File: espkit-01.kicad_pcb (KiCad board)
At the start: 2 copper layers, 20 x 25 mm, 14 parts, among them IC1 WS2812B, P1 ESP-01, P2 BREAKOUT, P3 SERIAL, P4 PWR, P5 NEOPIXEL, P6 BRIDGE, SW1 RESET, SW2 PRGM

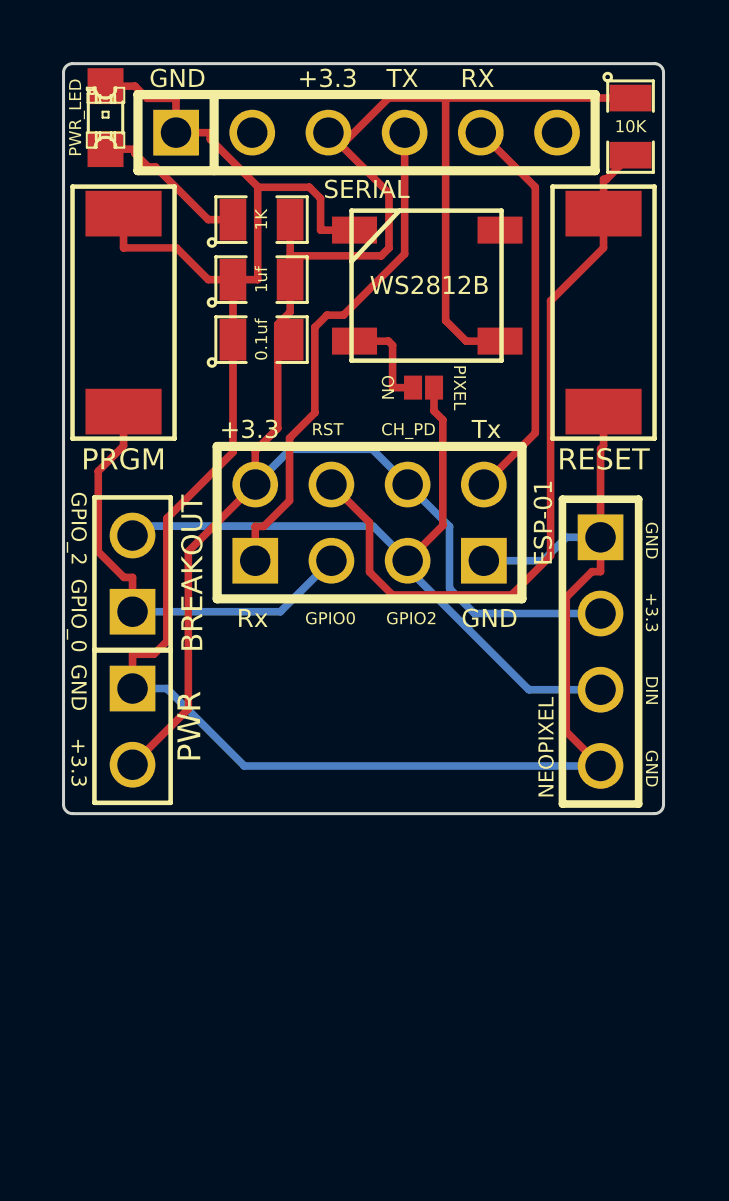
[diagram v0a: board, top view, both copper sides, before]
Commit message: Redundant power led removed
bridge connection now easy to get too.
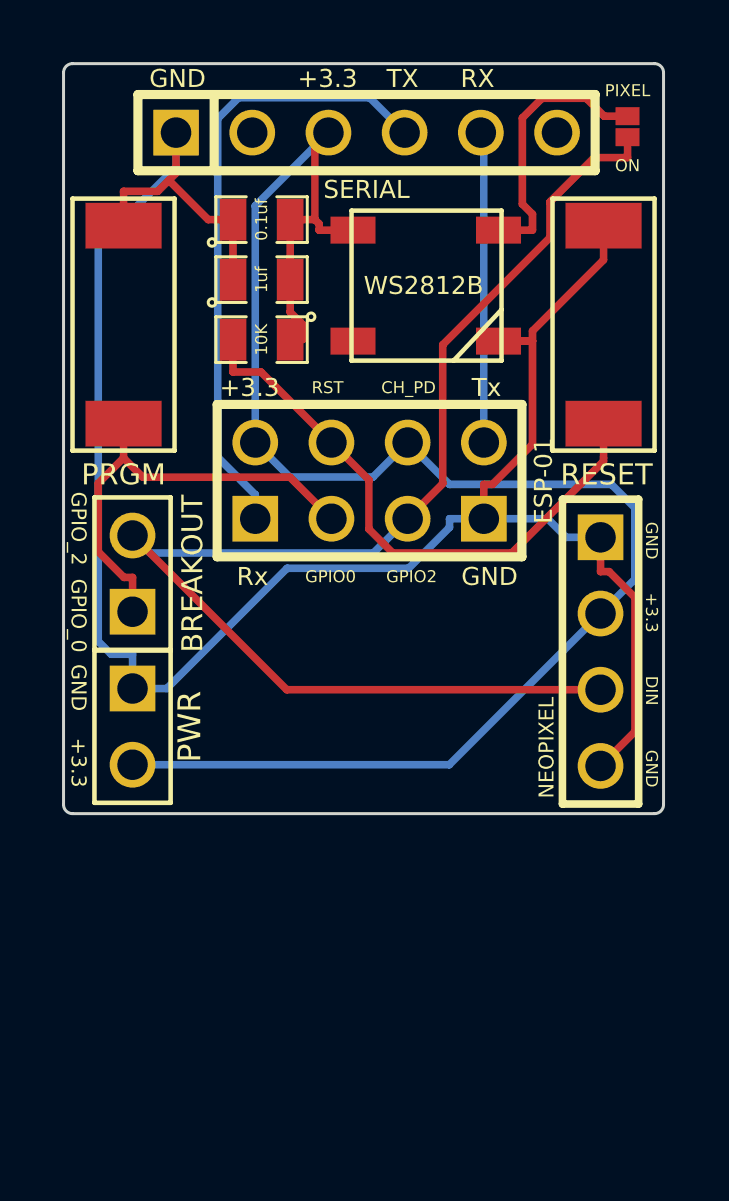
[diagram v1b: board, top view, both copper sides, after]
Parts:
- removed D1: PWR_LED, LED-0805
- removed R3: 1K, SM0805
- moved R1 14.2 mm to (18.7, 21.3), turned to 180 degrees
- moved P6 11.0 mm to (30.9, 14.2), turned to 90 degrees
- moved C2 4.00 mm to (18.7, 17.3)
- moved P1 1.40 mm to (22.3, 26.0)
- moved SW1 0.40 mm to (30.1, 20.8), turned to 270 degrees
- moved SW2 0.40 mm to (14.1, 20.8)
- turned IC1 to 0 degrees
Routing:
- net GPIO2: track 24.5 -> 44.0 mm
- net +3.3V: track 64.1 -> 57.6 mm
- net N-000004: track 3.42 -> 9.03 mm
- net N-0000012: track 24.9 -> 19.4 mm
- net N-000006: track 5.31 -> 0.00 mm
- net TX: track 16.8 -> 21.6 mm
- net RX: track 13.2 -> 10.4 mm
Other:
- board text added: "ESPkit-01 V1.2 https://github.com/mage0r/ESPkit-01 John Spencer & Andy Gelme, 2015 Made at hackmelbourne.org"
- board text removed: "ESPkit-01 V1.1 https://github.com/mage0r/ESPkit-01 John Spencer & Andy Gelme, 2015 Made at hackmelbourne.org"

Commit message: New Design with auto program.
You should be able to do away with the serial/usb programmer and just use the NodeMCU v1.0 board in Arduino to auto-program.
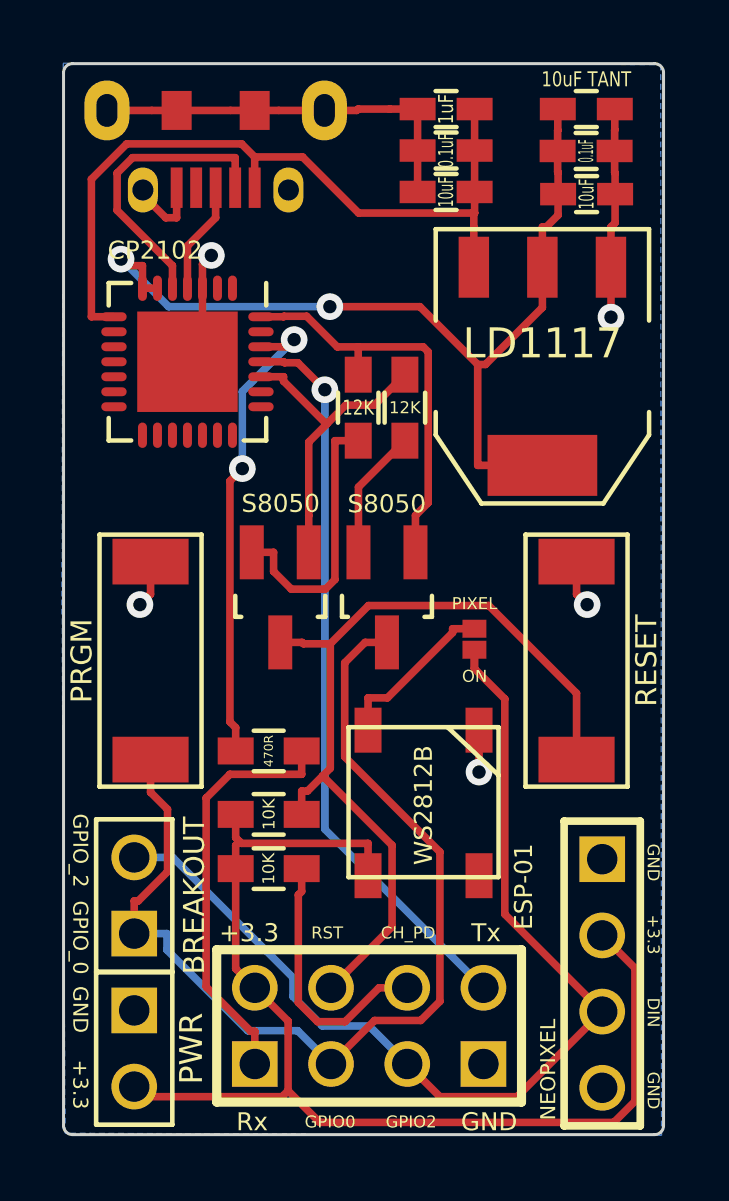
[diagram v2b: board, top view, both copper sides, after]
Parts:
- removed C2: 0.1uf, SM0805
- removed C3: 1uf, SM0805
- added C1: 10uF, Capacitors_SMD:C_0603_HandSoldering, F.Cu at (29.5, 16.4)
- added C4: 0.1uF, Capacitors_SMD:C_0603_HandSoldering, F.Cu at (29.5, 15.0)
- added C5: 1uF, Capacitors_SMD:C_0603_HandSoldering, F.Cu at (24.9, 13.6)
- added C6: 10uF, Capacitors_SMD:C_0603_HandSoldering, F.Cu at (24.9, 16.4)
- added C7: 0.1uF, Capacitors_SMD:C_0603_HandSoldering, F.Cu at (24.9, 15.0)
- added C8: 10uF TANT, Capacitors_SMD:C_0603_HandSoldering, F.Cu at (29.5, 13.6)
- added Q1: S8050, TO_SOT_Packages_SMD:SOT-23_Handsoldering, F.Cu at (19.3, 29.9)
- added Q2: S8050, TO_SOT_Packages_SMD:SOT-23_Handsoldering, F.Cu at (22.9, 29.9)
- added R2: 12K, Resistors_SMD:R_0603_HandSoldering, F.Cu at (21.9, 23.6)
- added R3: 12K, Resistors_SMD:R_0603_HandSoldering, F.Cu at (23.5, 23.6)
- added R4: 10K, Resistors_SMD:R_0603_HandSoldering, F.Cu at (18.9, 37.1)
- added R5: 470R, Resistors_SMD:R_0603_HandSoldering, F.Cu at (18.9, 35.0)
- added U1: LD1117, TO_SOT_Packages_SMD:SOT-223, F.Cu at (28.1, 22.2)
- added U2: CP2102, Housings_DFN_QFN:QFN-28-1EP_5x5mm_Pitch0.5mm, F.Cu at (16.2, 22.0)
- P3: value SERIAL -> USB_5PIN_SHELL; footprint PIN_ARRAY-6X1 -> freetronics_footprints:USB-MICRO-5pin_PTHMOUNT
- R1: footprint SM0805 -> Resistors_SMD:R_0603_HandSoldering
- moved P1 18.2 mm to (22.3, 44.2)
- moved P6 17.8 mm to (25.8, 31.3)
- moved R1 17.6 mm to (18.9, 38.9)
- moved IC1 17.2 mm to (24.1, 36.7), turned to 90 degrees
- moved SW1 11.2 mm to (29.2, 32.0)
- moved SW2 11.2 mm to (15.0, 32.0), turned to 270 degrees
- moved P5 10.7 mm to (30.1, 42.4)
- moved P2 10.7 mm to (14.5, 39.8)
- moved P4 10.7 mm to (14.5, 44.9)
- moved P3 5.35 mm to (17.2, 16.2), turned to 270 degrees
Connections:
- net GPIO2 renamed /GPIO2
- IC1 pad 2: (no net) -> Net-(IC1-Pad2)
- P1 pad 1: TX -> /TXD
- P1 pad 3: GPIO0 -> /GPIO0
- P1 pad 4: N-0000012 -> /RESET
- P1 pad 6: +3.3V -> /ESP_EN
- P1 pad 8: RX -> /RXD
- P2 pad 1: GPIO0 -> /GPIO0
- P3 pad 1: GND -> +5V
- P3 pad 2: (no net) -> /USB_D-
- P3 pad 3: +3.3V -> /USB_D+
- P3 pad 4: TX -> Net-(P3-Pad4)
- P3 pad 5: RX -> GND
- R1 pad 1: +3.3V -> /ESP_EN
- R1 pad 2: N-0000012 -> +3.3V
- SW1 pad 1: N-0000012 -> /RESET
- SW2 pad 1: GND -> /GPIO0
- SW2 pad 2: GPIO0 -> GND
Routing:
- net GND: track 70.6 -> 35.4 mm, vias 0 -> 5
- net /GPIO0: track 0.00 -> 34.0 mm
- net +3V3: track 0.00 -> 30.8 mm, vias 0 -> 2
- net /RESET: track 0.00 -> 28.9 mm
- net +5V: track 0.00 -> 25.9 mm
- net /RXD: track 0.00 -> 24.6 mm, vias 0 -> 1
- net TX: track 21.6 -> 0.00 mm
- net N-0000012: track 19.4 -> 0.00 mm
- net +3.3V: track 57.6 -> 39.0 mm
- net Net-(R5-Pad2): track 0.00 -> 15.9 mm, vias 0 -> 2
- net GPIO0: track 15.0 -> 0.00 mm
- net /TXD: track 0.00 -> 13.9 mm
- net /DTR: track 0.00 -> 13.9 mm
- net /RTS: track 0.00 -> 10.7 mm
- net RX: track 10.4 -> 0.00 mm
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- added copper zone on B.Cu, net GND
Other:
- board size 20 x 25 mm -> 20 x 35.7 mm
- net class 2.0mm added: clearance 0.2, trace_width 0.2, via_dia 0.889, via_drill 0.635
- net class Default: clearance 0.254 -> 0.2
- rule trace_clearance: 0.254 -> 0.2
- rule trace_min: 0.254 -> 0.2
- board text added: "ESPkit-01 V1.3 https://github.com/mage0r/ESPkit-01 John Spencer & Andy Gelme, 2016 Made at hackmelbourne.org"
- board text removed: "3.3V ONLY!"
- board text removed: "ESPkit-01 V1.2 https://github.com/mage0r/ESPkit-01 John Spencer & Andy Gelme, 2015 Made at hackmelbourne.org"
- board text removed: "RX"
- board text removed: "TX"
